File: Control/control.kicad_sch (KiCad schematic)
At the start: 34 parts, among them J2-J1 Conn_01x10, J3 Conn_01x01, J3-J1 Conn_01x10, J4 Conn_01x01, U1 TLV2372, U2 TLV2372, U3 ACS71240KEXBLT-050U5, U4 ACS71240KEXBLT-010B3, U6 LP-MSPM0G3507

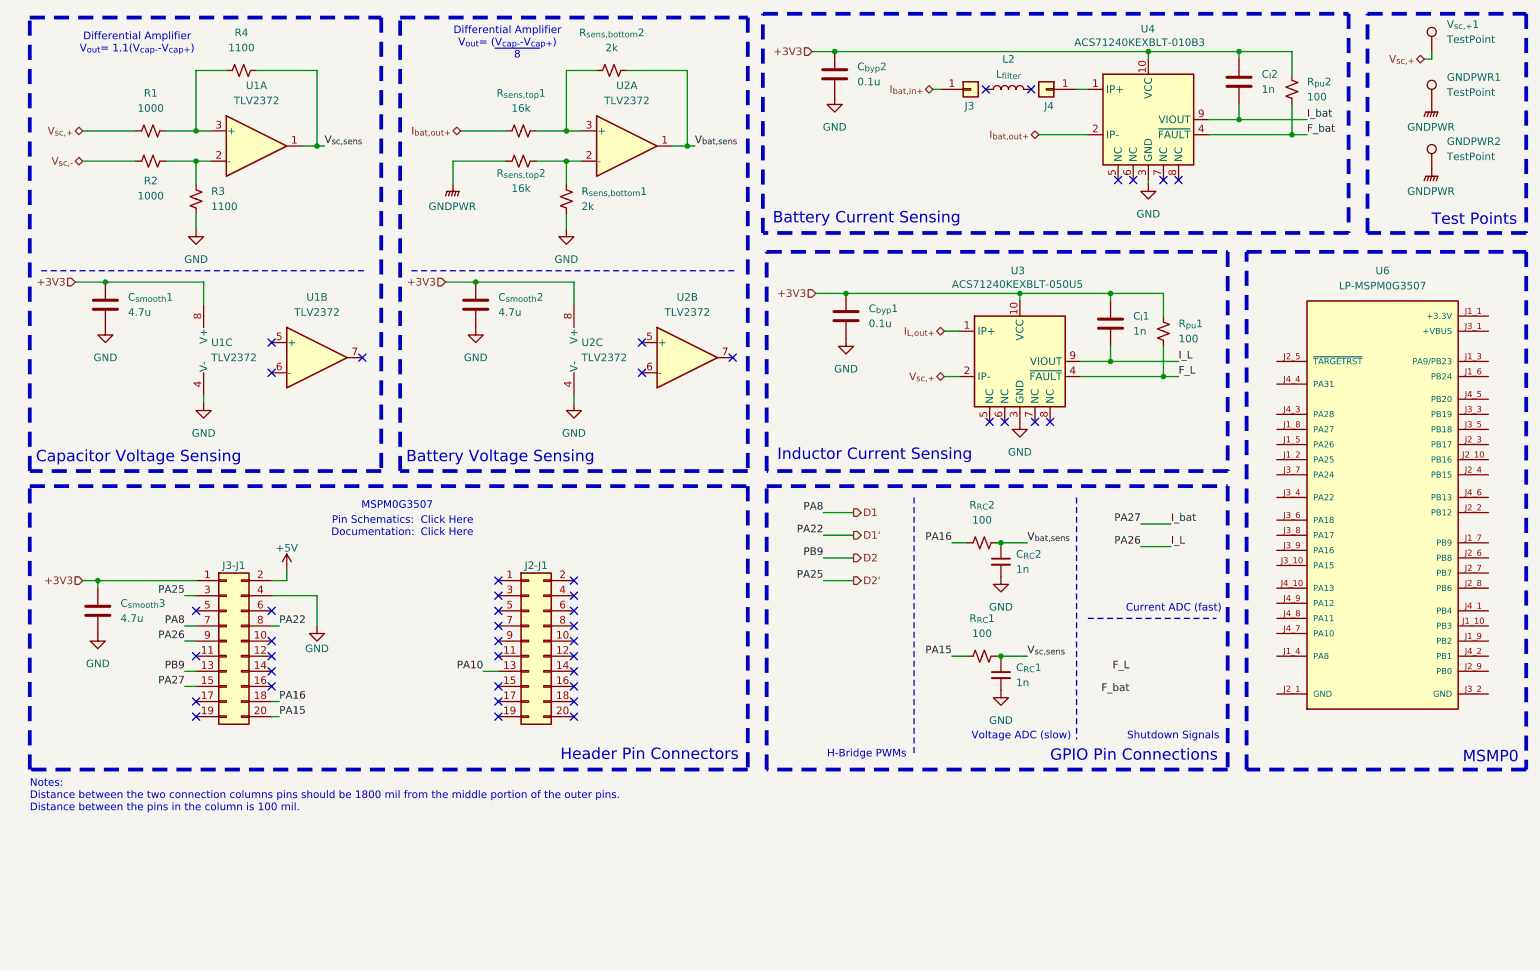
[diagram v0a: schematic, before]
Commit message: Fault Code & Pins
Added the config for the hardware fault handing of the current sensors. When the fault signal falls low all pwm signals and their complements are set to grounod. Additionally the traces for this were run on the board.

Other: Changed some ADC input pins to avoid double use with the launch pad board.
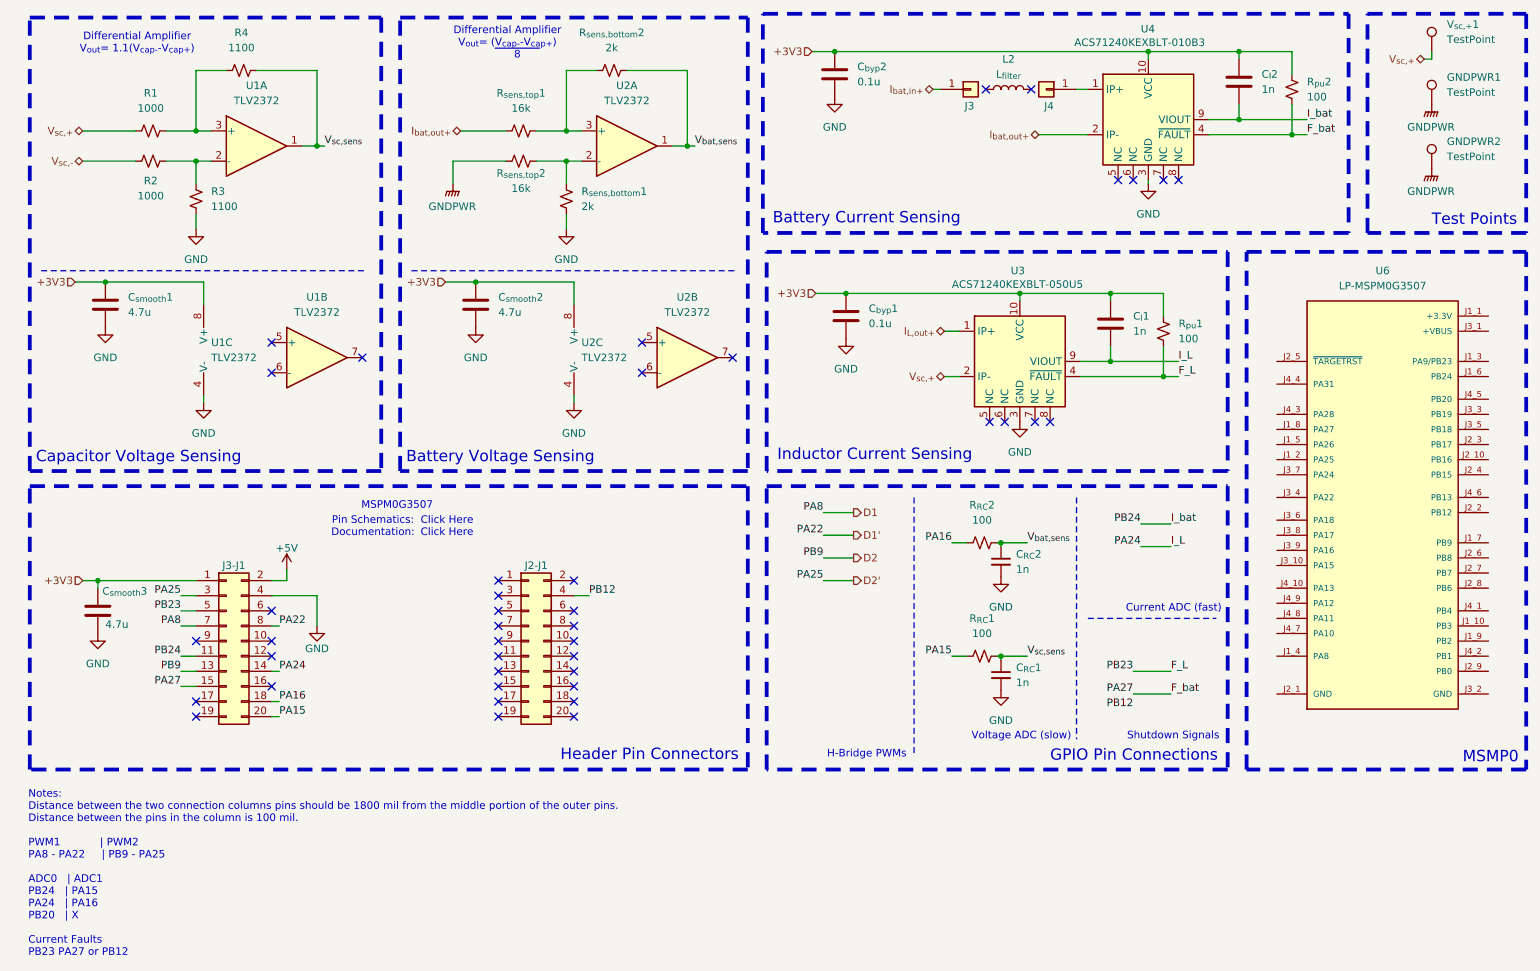
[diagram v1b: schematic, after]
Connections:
- net F_L: now also J3-J1.5 (Pin_5)
- net F_bat: now also J3-J1.15 (Pin_15)
- net I_L: now also J3-J1.14 (Pin_14); no longer J3-J1.9 (Pin_9)
- net I_bat: now also J3-J1.11 (Pin_11); no longer J3-J1.15 (Pin_15)
- net PB12: now reaches J2-J1.4 (Pin_4)
- net PA10: no longer names the net of J2-J1.13 (Pin_13)
- no-connect marks 44 -> 42
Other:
- note added: "Notes: Distance between the two connection columns pins should be 1800 mil from the middle portion of the outer pins. Distance between the pins in the column is 100 mil. PWM1 | PWM2 PA8 - PA22 | PB9 - PA25 ADC0 | ADC1 PB24 | PA15 PA24 | PA16 PB20 | X Current Faults PB23 PA27 or PB12"
- note removed: "Notes: Distance between the two connection columns pins should be 1800 mil from the middle portion of the outer pins. Distance between the pins in the column is 100 mil."
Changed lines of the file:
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@@
 		)
 	)
-	(text "Notes: \nDistance between the two connection columns pins should be 1800 mil from the middle portion of the outer pins.\nDistance between the pins in the column is 100 mil. "
+	(text "Notes: \nDistance between the two connection columns pins should be 1800 mil from the middle portion of the outer pins.\nDistance between the pins in the column is 100 mil. \n\nPWM1            | PWM2  \nPA8 - PA22     | PB9 - PA25\n\nADC0   | ADC1\nPB24   | PA15\nPA24   | PA16\nPB20   | X\n\nCurrent Faults\nPB23 PA27 or PB12\n\n\n"
 		(exclude_from_sim no)
-		(at 21.59 168.275 0)
+		(at 21.336 183.388 0)
 		(effects
 			(font
@@
 	)
 	(no_connect
-		(at 62.23 147.32)
-	)
-	(no_connect
 		(at 100.33 132.08)
 	)
@@
 	)
 	(no_connect
+		(at 49.53 142.24)
+	)
+	(no_connect
 		(at 100.33 152.4)
 	)
@@
 	)
 	(no_connect
-		(at 49.53 137.16)
-	)
-	(no_connect
 		(at 62.23 137.16)
 	)
@@
 	)
 	(no_connect
-		(at 49.53 152.4)
+		(at 100.33 147.32)
 	)
 	(no_connect
-		(at 49.53 144.78)
+		(at 49.53 152.4)
 	)
 	(no_connect
@@
 	)
 	(no_connect
-		(at 100.33 142.24)
-	)
-	(no_connect
 		(at 77.47 94.615)
 	)
 	(no_connect
-		(at 113.03 134.62)
+		(at 100.33 142.24)
 	)
 	(no_connect
@@
 	(wire
 		(pts
-			(xy 47.625 139.7) (xy 49.53 139.7)
+			(xy 46.99 139.7) (xy 49.53 139.7)
 		)
 		(stroke
@@
 	(wire
 		(pts
+			(xy 207.01 151.13) (xy 213.36 151.13)
+		)
+		(stroke
+			(width 0)
+			(type default)
+		)
+	)
+	(wire
+		(pts
 			(xy 203.2 85.09) (xy 203.2 83.82)
 		)
@@
 	(wire
 		(pts
-			(xy 47.625 134.62) (xy 49.53 134.62)
+			(xy 115.57 134.62) (xy 113.03 134.62)
 		)
 		(stroke
@@
 	(wire
 		(pts
-			(xy 184.785 144.78) (xy 189.23 144.78)
+			(xy 46.99 134.62) (xy 49.53 134.62)
 		)
 		(stroke
@@
 	(wire
 		(pts
-			(xy 69.85 59.055) (xy 71.12 59.055)
+			(xy 184.785 144.78) (xy 189.23 144.78)
 		)
 		(stroke
@@
 	(wire
 		(pts
-			(xy 54.61 46.355) (xy 49.53 46.355)
+			(xy 69.85 59.055) (xy 71.12 59.055)
 		)
 		(stroke
@@
 	(wire
 		(pts
-			(xy 47.625 142.24) (xy 49.53 142.24)
+			(xy 54.61 46.355) (xy 49.53 46.355)
 		)
 		(stroke
 			(width 0)
-			(type solid)
+			(type default)
 		)
 	)
@@
 	(wire
 		(pts
-			(xy 97.79 147.32) (xy 100.33 147.32)
+			(xy 156.845 43.18) (xy 209.55 43.18)
 		)
 		(stroke
@@
 	(wire
 		(pts
-			(xy 156.845 43.18) (xy 209.55 43.18)
+			(xy 59.69 46.355) (xy 69.85 46.355)
 		)
 		(stroke
@@
 	(wire
 		(pts
-			(xy 59.69 46.355) (xy 69.85 46.355)
+			(xy 46.99 137.16) (xy 49.53 137.16)
 		)
 		(stroke
@@
 		)
 	)
+	(wire
+		(pts
+			(xy 207.01 147.32) (xy 213.36 147.32)
+		)
+		(stroke
+			(width 0)
+			(type default)
+		)
+	)
 	(polyline
 		(pts
@@
 	(wire
 		(pts
+			(xy 62.23 147.32) (xy 63.5 147.32)
+		)
+		(stroke
+			(width 0)
+			(type default)
+		)
+	)
+	(wire
+		(pts
 			(xy 233.68 46.99) (xy 233.68 43.18)
 		)
@@
 	(wire
 		(pts
-			(xy 47.625 149.86) (xy 49.53 149.86)
+			(xy 46.99 144.78) (xy 49.53 144.78)
 		)
 		(stroke
@@
 	(wire
 		(pts
-			(xy 47.625 147.32) (xy 49.53 147.32)
+			(xy 46.99 147.32) (xy 49.53 147.32)
 		)
 		(stroke
@@
 	(wire
 		(pts
+			(xy 46.99 149.86) (xy 49.53 149.86)
+		)
+		(stroke
+			(width 0)
+			(type default)
+		)
+	)
+	(wire
+		(pts
 			(xy 92.71 61.595) (xy 101.6 61.595)
 		)
@@
 		)
 	)
-	(label "PA27"
+	(label "PB24"
+		(at 46.99 144.78 180)
+		(effects
+			(font
+				(size 1.27 1.27)
+			)
+			(justify right bottom)
+		)
+	)
+	(label "PB24"
 		(at 208.28 122.555 180)
 		(effects
@@
 		)
 	)
+	(label "PB23"
+		(at 207.01 147.32 180)
+		(effects
+			(font
+				(size 1.27 1.27)
+			)
+			(justify right bottom)
+		)
+	)
 	(label "V_{sc,sens}"
 		(at 189.23 144.78 0)
@@
 		)
 	)
-	(label "F_L"
-		(at 206.375 147.32 180)
+	(label "PA27"
+		(at 207.01 151.13 180)
 		(effects
 			(font
@@
 		)
 	)
+	(label "F_L"
+		(at 213.36 147.32 0)
+		(effects
+			(font
+				(size 1.27 1.27)
+			)
+			(justify left bottom)
+		)
+	)
 	(label "V_{sc,sens}"
 		(at 71.12 59.055 0)
@@
 	)
 	(label "PA25"
-		(at 47.625 134.62 180)
+		(at 46.99 134.62 180)
 		(effects
 			(font
@@
 		)
 	)
-	(label "PA16"
-		(at 176.53 125.73 180)
+	(label "PB12"
+		(at 207.01 153.67 180)
 		(effects
 			(font
@@
 	)
 	(label "PA16"
-		(at 63.5 152.4 0)
+		(at 176.53 125.73 180)
 		(effects
 			(font
 				(size 1.27 1.27)
 			)
-			(justify left bottom)
+			(justify right bottom)
 		)
 	)
-	(label "PB9"
-		(at 154.94 128.27 180)
+	(label "PA16"
+		(at 63.5 152.4 0)
 		(effects
 			(font
 				(size 1.27 1.27)
 			)
-			(justify right bottom)
+			(justify left bottom)
 		)
 	)
 	(label "PB9"
-		(at 47.625 147.32 180)
+		(at 154.94 128.27 180)
 		(effects
 			(font
@@
 		)
 	)
-	(label "PA27"
-		(at 47.625 149.86 180)
+	(label "PB9"
+		(at 46.99 147.32 180)
 		(effects
 			(font
@@
 		)
 	)
-	(label "PA10"
-		(at 97.79 147.32 180)
+	(label "PB23"
+		(at 46.99 137.16 180)
 		(effects
 			(font
@@
 		)
 	)
+	(label "PB12"
+		(at 115.57 134.62 0)
+		(effects
+			(font
+				(size 1.27 1.27)
+			)
+			(justify left bottom)
+		)
+	)
 	(label "I_L"
 		(at 213.36 126.365 0)
@@
 	)
 	(label "PA8"
-		(at 47.625 139.7 180)
+		(at 46.99 139.7 180)
 		(effects
 			(font
@@
 		)
 	)
-	(label "PA26"
-		(at 47.625 142.24 180)
+	(label "PA24"
+		(at 63.5 147.32 0)
+		(effects
+			(font
+				(size 1.27 1.27)
+			)
+			(justify left bottom)
+		)
+	)
+	(label "PA27"
+		(at 46.99 149.86 180)
 		(effects
 			(font
@@
 		)
 	)
-	(label "PA26"
+	(label "PA24"
 		(at 208.28 126.365 180)
 		(effects
@@
 	)
 	(label "F_bat"
-		(at 206.375 151.13 180)
+		(at 213.36 151.13 0)
 		(effects
 			(font
 				(size 1.27 1.27)
 			)
-			(justify right bottom)
+			(justify left bottom)
 		)
 	)
@@
 			)
 		)
-		(property "Datasheet" "~"
+		(property "Datasheet" ""
 			(at 184.785 147.955 0)
 			(effects
@@
 			)
 		)
-		(property "Datasheet" "~"
+		(property "Datasheet" ""
 			(at 262.255 43.18 0)
 			(effects
@@
 			)
 		)
-		(property "Datasheet" "~"
+		(property "Datasheet" ""
 			(at 192.405 49.53 0)
 			(effects
@@
 			)
 		)
-		(property "Datasheet" "~"
+		(property "Datasheet" ""
 			(at 262.255 62.865 0)
 			(effects
@@
 			)
 		)
-		(property "Datasheet" "~"
+		(property "Datasheet" ""
 			(at 179.705 49.53 0)
 			(effects
@@
 			)
 		)
-		(property "Datasheet" "~"
+		(property "Datasheet" ""
 			(at 54.61 142.24 0)
 			(effects
@@
 			)
 		)
-		(property "Datasheet" "~"
+		(property "Datasheet" ""
 			(at 184.785 128.905 0)
 			(effects
@@
 		(dnp no)
 		(property "Reference" "C_{smooth}3"
-			(at 36.83 135.8899 0)
+			(at 33.782 133.858 0)
 			(effects
 				(font
@@
 		)
 		(property "Value" "4.7u"
-			(at 36.83 138.4299 0)
+			(at 34.29 139.446 0)
 			(effects
 				(font
@@
 			)
 		)
-		(property "Datasheet" "~"
+		(property "Datasheet" ""
 			(at 105.41 142.24 0)
 			(effects
@@
 			)
 		)
-		(property "Datasheet" "~"
+		(property "Datasheet" ""
 			(at 262.255 52.07 0)
 			(effects

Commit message: big ahhhh merge + partial bringup guide written
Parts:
- removed C_{byp}1: 0.1u, Capacitor_SMD:C_0603_1608Metric_Pad1.08x0.95mm_HandSolder, symbol Device:C
- removed C_{l}1: 1n, Capacitor_SMD:C_0603_1608Metric_Pad1.08x0.95mm_HandSolder, symbol Device:C
- removed R_{pu}1: 100, Resistor_SMD:R_0603_1608Metric_Pad0.98x0.95mm_HandSolder, symbol Device:R_Small_US
- removed U3: ACS71240KEXBLT-050U5, Sensor_Current:Allegro_QFN-12-10-1EP_3x3mm_P0.5mm, symbol Sensor_Current:ACS711xEXLT-31AB
- added C_{d}1, C_{d}2: 0.1u, Capacitor_SMD:C_0603_1608Metric_Pad1.08x0.95mm_HandSolder, symbol Device:C
- added C_{filter}1, C_{filter}2, C_{filter}3, C_{filter}4: 10u, Capacitor_SMD:C_0603_1608Metric_Pad1.08x0.95mm_HandSolder, symbol Device:C
- added R_{filter}1: 3.3, Resistor_SMD:R_0603_1608Metric_Pad0.98x0.95mm_HandSolder, symbol Device:R_US
- J2-J1, J3-J1: Digi-Key Part Number (none) -> 2553-2044-2X10G00SA-ND; Manufacturer_Part_Number (none) -> 2044-2X10G00SA
- L1: renamed from L2; value L_{filter} -> 41u
- R1, R2: value 1000 -> 10k; Manufacturer_Part_Number RT0603DRD071KL -> RN73R1JTTD1002B50; Mouser Part Number 603-RT0603DRD071KL -> 660-RN73R1JTD1002B50
- R3, R4: value 1100 -> 11k; Manufacturer_Part_Number RT0603DRD071K1L -> RN73R1JTTD1102B25; Mouser Part Number 603-RT0603DRD071K1L -> 660-RN73R1JTD1102B25
- R_{sens,top}1, R_{sens,top}2: Manufacturer_Part_Number RT0603DRE0716KL -> RT0603DRD0716KL; Mouser Part Number 603-RT0603DRE0716KL -> 603-RT0603DRD0716KL
- U1: value TLV2372 -> TLV9152IDR; Manufacturer_Part_Number (none) -> TLV9152IDR; Mouser Part Number (none) -> 595-TLV9152IDR; now in the parts list
- U2: value TLV2372 -> TLV9152IDR; Manufacturer_Part_Number (none) -> TLV9152IDR; Mouser Part Number (none) -> 595-TLV9152IDR
- U4: renamed from U6; now not fitted
- renumbered C_{RC}2 to C_{RC}1, C_{RC}1 to C_{RC}2, C_{byp}2 to C_{byp}1, C_{l}2 to C_{l}1, C_{smooth}3 to C_{smooth}2, C_{smooth}2 to C_{smooth}3, J3 to J1, J4 to J2, R_{RC}2 to R_{RC}1, R_{RC}1 to R_{RC}2, R_{pu}2 to R_{pu}1, U4 to U3
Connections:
- net +3V3: now also C_{d}1.1, C_{d}2.1
- net GND: now also C_{d}1.2, C_{d}2.2
- net GNDPWR: now also C_{filter}1.2, C_{filter}2.2, C_{filter}3.2, C_{filter}4.2
- net at J2.1 (Pin_1), U3.1 (IP+): now also R_{filter}1.1
- new net: C_{filter}1.1, C_{filter}2.1, C_{filter}3.1, C_{filter}4.1, R_{filter}1.2
- no-connect marks 42 -> 38
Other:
- note added: "Low-Pass Filter"
- note removed: "Inductor Current Sensing"
- moved on the sheet: C_{byp}1, C_{l}1, C_{smooth}1, C_{smooth}3, GNDPWR1, GNDPWR2, J1, J2, L1, R_{pu}1, U1B, U1C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
